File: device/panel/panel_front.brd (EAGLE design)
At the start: 143.5 x 70 mm, 1 part

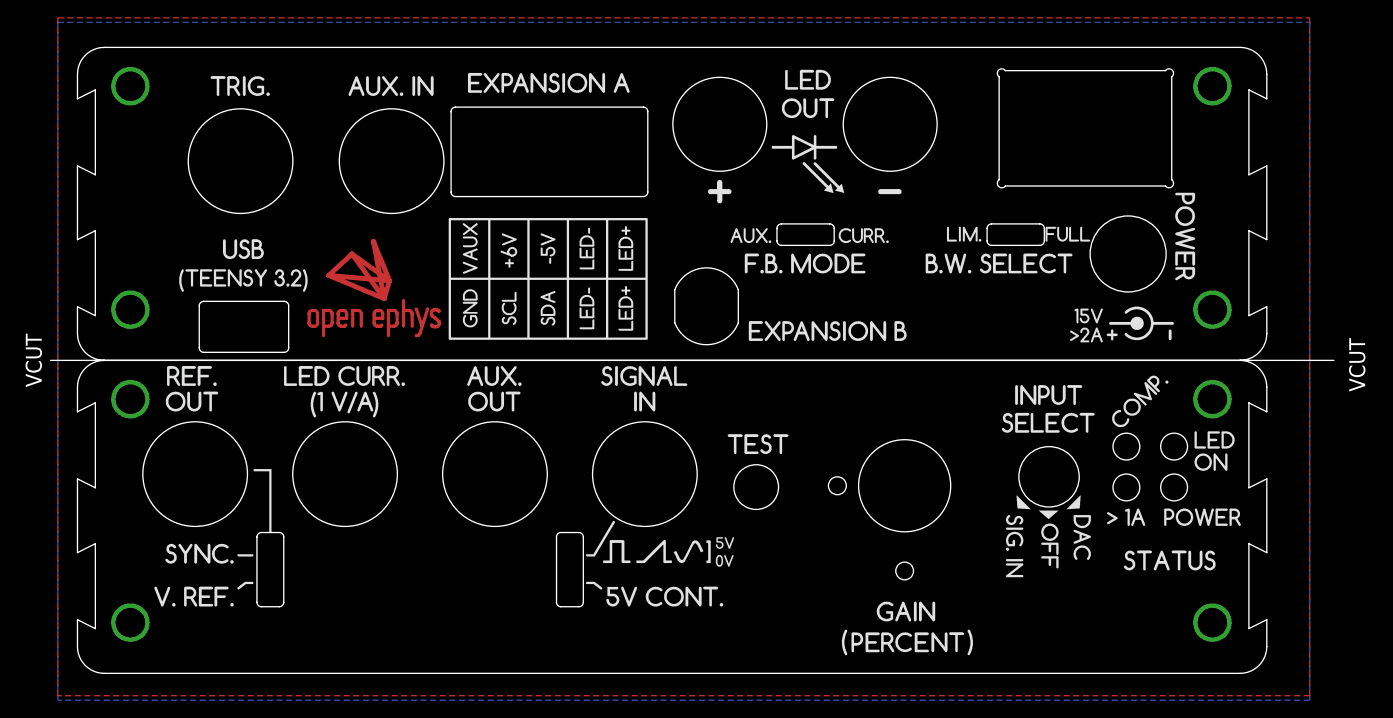
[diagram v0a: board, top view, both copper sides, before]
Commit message: Split panel into two files (front and back panel)
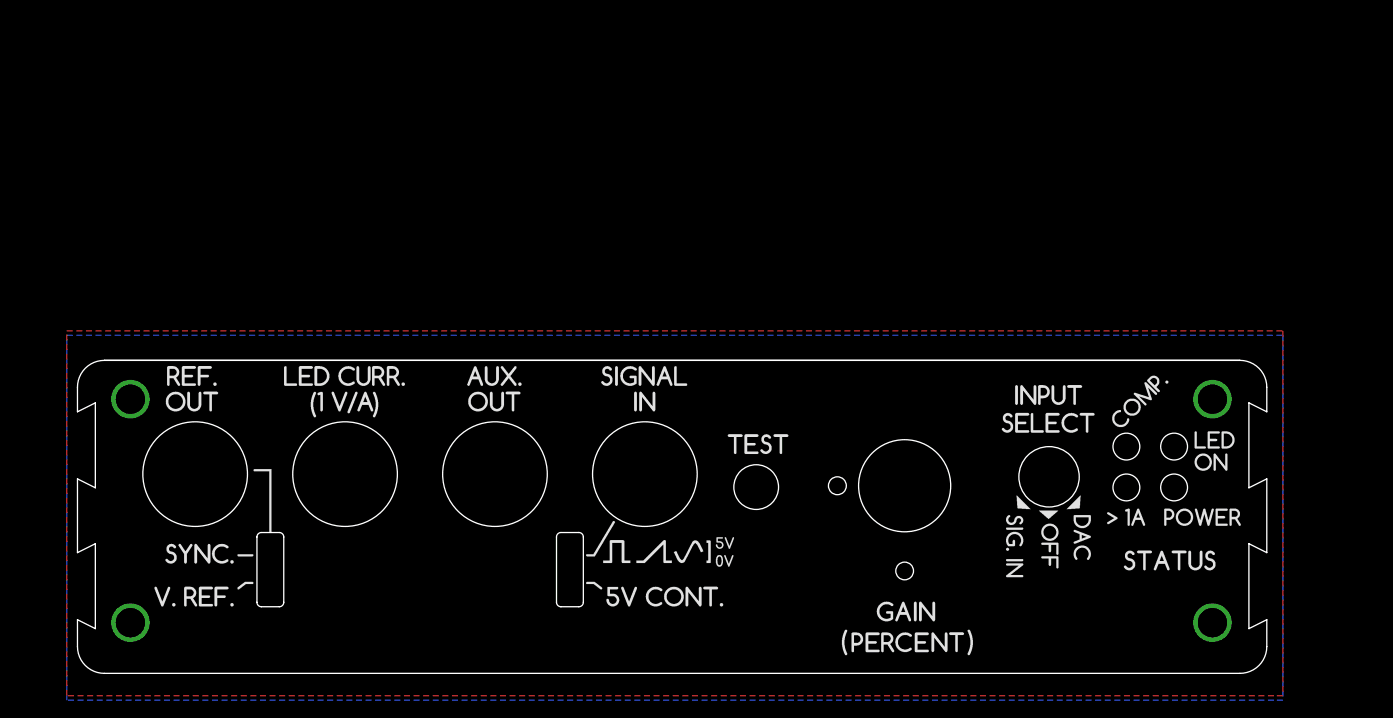
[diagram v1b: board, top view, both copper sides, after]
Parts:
- removed E$1: (no value), jonnew:OE-LOGO-14X10
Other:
- board size 143.5 x 70 mm -> 133 x 35 mm
- board text removed: "VCUT"
